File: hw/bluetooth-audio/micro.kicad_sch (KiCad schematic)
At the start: 24 parts, among them J4 Conn_01x02, U1 STM32WB55CGUx, Y1 32MHz, Y2 32.768KHz

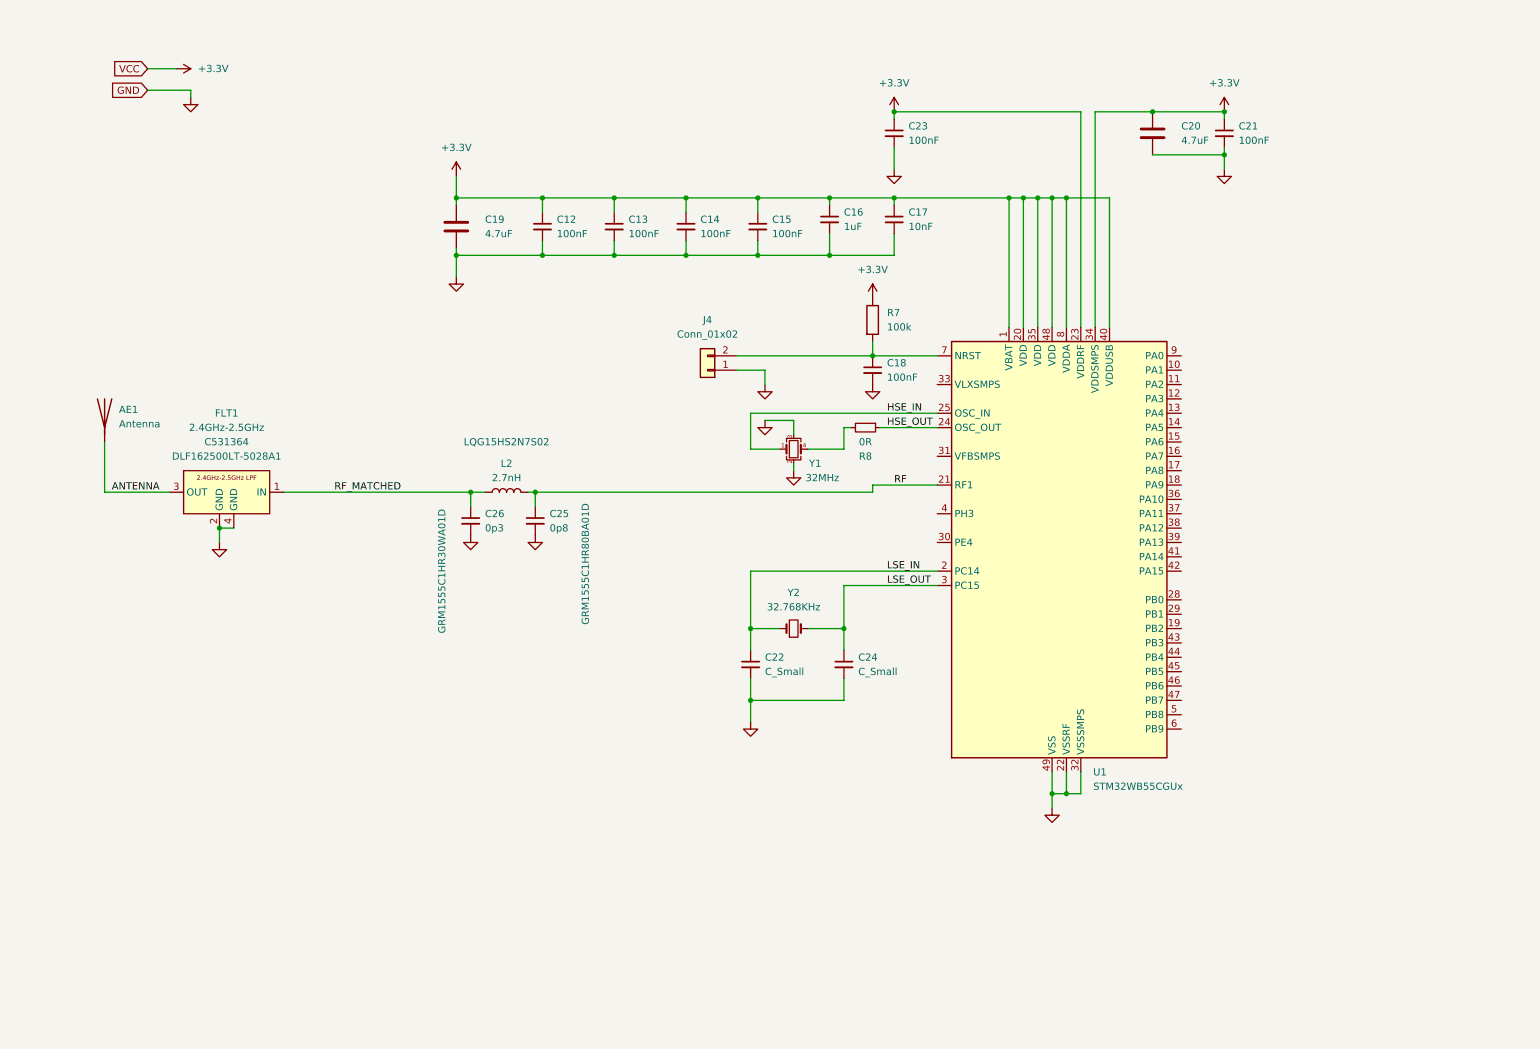
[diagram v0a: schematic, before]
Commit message: Completed design with ESP32D0WD-v3, and JLC production files. High production cost due to req of PCBA standard, due to ESP32 pin pitch.
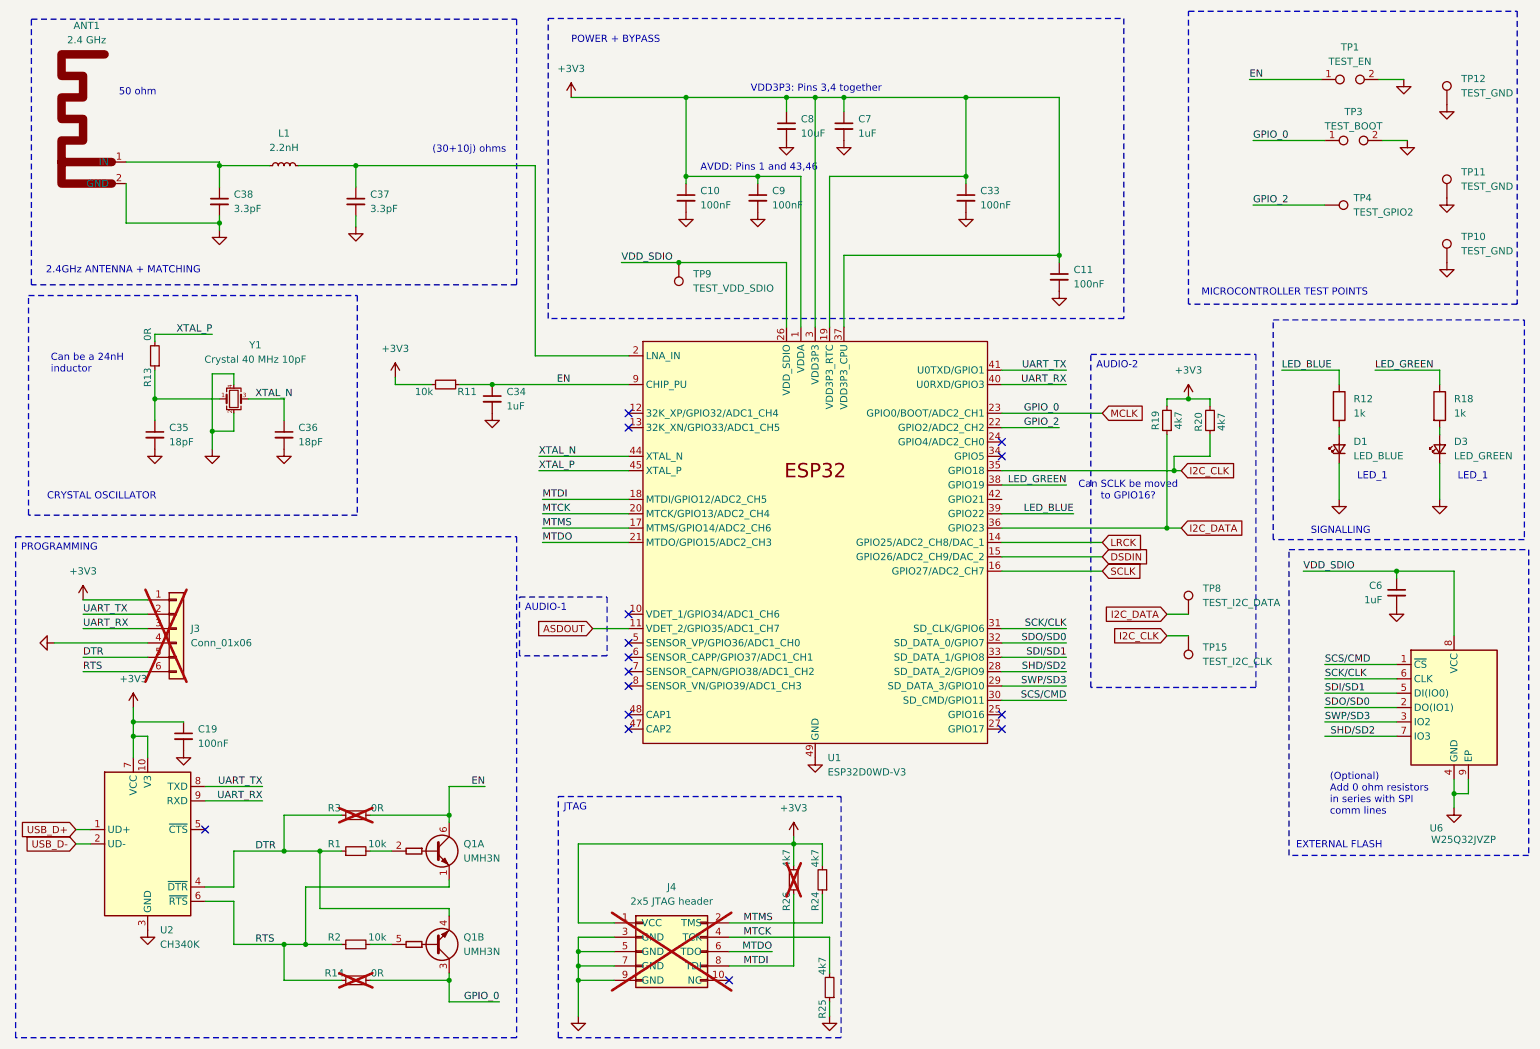
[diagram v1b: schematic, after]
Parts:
- removed AE1: Antenna, symbol Device:Antenna
- removed C12, C13, C14, C15, C18, C21, C23: 100nF, Resistor_SMD:R_0402_1005Metric, symbol Device:C_Small
- removed C16: 1uF, Resistor_SMD:R_0402_1005Metric, symbol Device:C_Small
- removed C17: 10nF, Resistor_SMD:R_0402_1005Metric, symbol Device:C_Small
- removed C19, C20: 4.7uF, Capacitor_SMD:C_0603_1608Metric, symbol Device:C
- removed C22, C24: C_Small, symbol Device:C_Small
- removed C25: 0p8, Inductor_SMD:L_0402_1005Metric, symbol Device:C_Small
- removed C26: 0p3, Inductor_SMD:L_0402_1005Metric, symbol Device:C_Small
- removed FLT1: 2.4GHz-2.5GHz, custom_footprints:DLF162500LT-5028A1, symbol custom_symbols:DLF162500LT-5028A1
- removed J4: Conn_01x02, symbol Connector_Generic:Conn_01x02
- removed L2: 2.7nH, Inductor_SMD:L_0402_1005Metric, symbol Device:L
- removed R7: 100k, symbol Device:R
- removed R8: 0R, symbol Device:R_Small
- removed U1: STM32WB55CGUx, Package_DFN_QFN:QFN-48-1EP_7x7mm_P0.5mm_EP5.6x5.6mm, symbol MCU_ST_STM32WB:STM32WB55CGUx
- removed Y1: 32MHz, symbol Device:Crystal_GND23_Small
- removed Y2: 32.768KHz, symbol Device:Crystal_Small
- added ANT1: 2.4 GHz, custom_footprints:Antenna 2.4GHz Inverted-F Meandered, symbol custom_symbols:Antenna_2.4GHz_Meandered_Inverted-F
- added C10, C11, C19, C33, C9: 100nF, Capacitor_SMD:C_0402_1005Metric, symbol Device:C_Small
- added C34, C6, C7: 1uF, Capacitor_SMD:C_0402_1005Metric, symbol Device:C_Small
- added C35, C36: 18pF, Capacitor_SMD:C_0402_1005Metric, symbol Device:C_Small
- added C37, C38: 3.3pF, Capacitor_SMD:C_0402_1005Metric, symbol Device:C_Small
- added C8: 10uF, Capacitor_SMD:C_0603_1608Metric, symbol Device:C_Small
- added D1: LED_BLUE, LED_SMD:LED_0805_2012Metric, symbol Device:LED_Small
- added D3: LED_GREEN, LED_SMD:LED_0805_2012Metric, symbol Device:LED_Small
- added J3: Conn_01x06, Connector_PinHeader_2.54mm:PinHeader_1x06_P2.54mm_Vertical, symbol Connector_Generic:Conn_01x06
- added J4: 2x5 JTAG header, custom_footprints:2x5 2mm JTAG header pads only, symbol custom_symbols:2x5 JTAG header
- added L1: 2.2nH, Inductor_SMD:L_0402_1005Metric, symbol Device:L_Small
- added Q1: UMH3N, Package_TO_SOT_SMD:SOT-363_SC-70-6, symbol Transistor_BJT:UMH3N
- added R1, R11, R2: 10k, Resistor_SMD:R_0402_1005Metric, symbol Device:R_Small
- added R12, R18: 1k, Resistor_SMD:R_0402_1005Metric, symbol Device:R
- added R13, R14, R3: 0R, Resistor_SMD:R_0402_1005Metric, symbol Device:R_Small
- added R19, R20, R24, R25, R26: 4k7, Resistor_SMD:R_0402_1005Metric, symbol Device:R_Small
- added TP1: TEST_EN, custom_footprints:TestPoint_Pad_2x1_D1.0mm, symbol Connector:TestPoint_2Pole
- added TP10, TP11, TP12: TEST_GND, TestPoint:TestPoint_Pad_D1.0mm, symbol Connector:TestPoint
- added TP15: TEST_I2C_CLK, TestPoint:TestPoint_Pad_D1.0mm, symbol Connector:TestPoint
- added TP3: TEST_BOOT, custom_footprints:TestPoint_Pad_2x1_D1.0mm, symbol Connector:TestPoint_2Pole
- added TP4: TEST_GPIO2, TestPoint:TestPoint_Pad_D1.0mm, symbol Connector:TestPoint
- added TP8: TEST_I2C_DATA, TestPoint:TestPoint_Pad_D1.0mm, symbol Connector:TestPoint
- added TP9: TEST_VDD_SDIO, TestPoint:TestPoint_Pad_D1.0mm, symbol Connector:TestPoint
- added U1: ESP32D0WD-V3, Package_DFN_QFN:QFN-48-1EP_5x5mm_P0.35mm_EP3.7x3.7mm_ThermalVias, symbol PCM_Espressif:ESP32
- added U2: CH340K, Package_SO:SSOP-10-1EP_3.9x4.9mm_P1mm_EP2.1x3.3mm, symbol Interface_USB:CH340K
- added U6: W25Q32JVZP, Package_SON:WSON-8-1EP_6x5mm_P1.27mm_EP3.4x4.3mm, symbol Memory_Flash:W25Q32JVZP
- added Y1: Crystal 40 MHz 10pF, Crystal:Crystal_SMD_SeikoEpson_FA128-4Pin_2.0x1.6mm, symbol Device:Crystal_GND24_Small
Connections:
- net GND: now also ANT1.2 (GND), C10.2, C11.2, C19.2, C33.2, C34.2, C35.2, C36.2, C37.2, C38.2, C6.2, C7.2, C8.2, C9.2, D1.1 (K), D3.1 (K), J3.4 (Pin_4), J4.3 (GND), J4.5 (GND), J4.7 (GND), J4.9 (GND), R25.1, TP1.2, TP10.1, TP11.1, TP12.1, TP3.2, U1.49 (GND), U2.11 (GND), U2.3 (GND), U6.4 (GND), U6.9 (EP), Y1.2, Y1.4
- new net: D3.2 (A), R18.2
- new net: C35.1, R13.1, Y1.1
- new net: Q1.5 (B2), R2.2
- new net: C37.1, L1.2, U1.2 (LNA_IN)
- new net: Q1.2 (B1), R1.2
- new net: D1.2 (A), R12.2
- new net: ANT1.1 (IN), C38.1, L1.1
- new net +3V3: C10.1, C11.1, C19.1, C33.1, C7.1, C8.1, C9.1, J3.1 (Pin_1), J4.1 (VCC), R11.2, R19.2, R20.2, R24.2, R26.2, U1.1 (VDDA), U1.19 (VDD3P3_RTC), U1.3 (VDD3P3), U1.37 (VDD3P3_CPU), U1.4 (VDD3P3), U1.43 (VDDA), U1.46 (VDDA), U2.10 (V3), U2.7 (VCC)
- new net ASDOUT: U1.11 (VDET_2/GPIO35/ADC1_CH7)
- new net DSDIN: U1.15 (GPIO26/ADC2_CH9/DAC_2)
- new net DTR: J3.5 (Pin_5), Q1.4 (E2), R1.1, R3.1, U2.4 (~{DTR})
- new net EN: C34.1, Q1.6 (C1), R11.1, R3.2, TP1.1, U1.9 (CHIP_PU)
- new net GPIO_2: TP4.1, U1.22 (GPIO2/ADC2_CH2)
- new net I2C_CLK: R20.1, TP15.1, U1.35 (GPIO18)
- new net I2C_DATA: R19.1, TP8.1, U1.36 (GPIO23)
- new net LED_BLUE: R12.1, U1.39 (GPIO22)
- new net LED_GREEN: R18.1, U1.38 (GPIO19)
- new net LRCK: U1.14 (GPIO25/ADC2_CH8/DAC_1)
- new net MCLK: Q1.3 (C2), R14.2, TP3.1, U1.23 (GPIO0/BOOT/ADC2_CH1)
- new net MTCK: J4.4 (TCK), R25.2, U1.20 (MTCK/GPIO13/ADC2_CH4)
- new net MTDI: J4.8 (TDI), R26.1, U1.18 (MTDI/GPIO12/ADC2_CH5)
- new net MTDO: J4.6 (TDO), U1.21 (MTDO/GPIO15/ADC2_CH3)
- new net MTMS: J4.2 (TMS), R24.1, U1.17 (MTMS/GPIO14/ADC2_CH6)
- new net RTS: J3.6 (Pin_6), Q1.1 (E1), R14.1, R2.1, U2.6 (~{RTS})
- new net SCK/CLK: U1.31 (SD_CLK/GPIO6), U6.6 (CLK)
- new net SCLK: U1.16 (GPIO27/ADC2_CH7)
- new net SCS/CMD: U1.30 (SD_CMD/GPIO11), U6.1 (~{CS})
- new net SDI/SD1: U1.33 (SD_DATA_1/GPIO8), U6.5 (DI(IO0))
- new net SDO/SD0: U1.32 (SD_DATA_0/GPIO7), U6.2 (DO(IO1))
- new net SHD/SD2: U1.28 (SD_DATA_2/GPIO9), U6.7 (IO3)
- new net SWP/SD3: U1.29 (SD_DATA_3/GPIO10), U6.3 (IO2)
- new net UART_RX: J3.3 (Pin_3), U1.40 (U0RXD/GPIO3), U2.9 (RXD)
- new net UART_TX: J3.2 (Pin_2), U1.41 (U0TXD/GPIO1), U2.8 (TXD)
- new net USB_D+: U2.1 (UD+)
- new net USB_D-: U2.2 (UD-)
- new net VDD_SDIO: C6.1, TP9.1, U1.26 (VDD_SDIO), U6.8 (VCC)
- new net XTAL_N: C36.1, U1.44 (XTAL_N), Y1.3
- new net XTAL_P: R13.2, U1.45 (XTAL_P)
- no-connect marks 0 -> 15
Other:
- note added: "(30+10j) ohms"
- note added: "(Optional) Add 0 ohm resistors in series with SPI comm lines"
- note added: "2.4GHz ANTENNA + MATCHING"
- note added: "50 ohm"
- note added: "AVDD: Pins 1 and 43,46"
- note added: "CRYSTAL OSCILLATOR"
- note added: "Can SCLK be moved to GPIO16?"
- note added: "Can be a 24nH inductor"
- note added: "EXTERNAL FLASH"
- note added: "LED_1"
- note added: "MICROCONTROLLER TEST POINTS"
- note added: "POWER + BYPASS"
- note added: "SIGNALLING"
- note added: "VDD3P3: Pins 3,4 together"

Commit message: Custom symbol and footprints for IS2083. Updated design document. Initial dump of components onto cleared PCB.
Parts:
- removed C10, C11, C19, C33, C9: 100nF, Capacitor_SMD:C_0402_1005Metric, symbol Device:C_Small
- removed C34, C6, C7: 1uF, Capacitor_SMD:C_0402_1005Metric, symbol Device:C_Small
- removed C35, C36: 18pF, Capacitor_SMD:C_0402_1005Metric, symbol Device:C_Small
- removed C8: 10uF, Capacitor_SMD:C_0603_1608Metric, symbol Device:C_Small
- removed J3: Conn_01x06, Connector_PinHeader_2.54mm:PinHeader_1x06_P2.54mm_Vertical, symbol Connector_Generic:Conn_01x06
- removed Q1: UMH3N, Package_TO_SOT_SMD:SOT-363_SC-70-6, symbol Transistor_BJT:UMH3N
- removed R1, R11, R2: 10k, Resistor_SMD:R_0402_1005Metric, symbol Device:R_Small
- removed R13, R14, R3: 0R, Resistor_SMD:R_0402_1005Metric, symbol Device:R_Small
- removed R19, R20: 4k7, Resistor_SMD:R_0402_1005Metric, symbol Device:R_Small
- removed TP15: TEST_I2C_CLK, TestPoint:TestPoint_Pad_D1.0mm, symbol Connector:TestPoint
- removed TP8: TEST_I2C_DATA, TestPoint:TestPoint_Pad_D1.0mm, symbol Connector:TestPoint
- removed TP9: TEST_VDD_SDIO, TestPoint:TestPoint_Pad_D1.0mm, symbol Connector:TestPoint
- removed U1: ESP32D0WD-V3, Package_DFN_QFN:QFN-48-1EP_5x5mm_P0.35mm_EP3.7x3.7mm_ThermalVias, symbol PCM_Espressif:ESP32
- removed U2: CH340K, Package_SO:SSOP-10-1EP_3.9x4.9mm_P1mm_EP2.1x3.3mm, symbol Interface_USB:CH340K
- removed U6: W25Q32JVZP, Package_SON:WSON-8-1EP_6x5mm_P1.27mm_EP3.4x4.3mm, symbol Memory_Flash:W25Q32JVZP
- removed Y1: Crystal 40 MHz 10pF, Crystal:Crystal_SMD_SeikoEpson_FA128-4Pin_2.0x1.6mm, symbol Device:Crystal_GND24_Small
- added U2: IS2083BM-232, custom_footprints:VFBGA82_3MX_MCH, symbol IS2083 Bluetooth Audio SoC:IS2083BM-232
- renumbered ANT1 to ANT2, C38 to C46, C37 to C48, D1 to D4, D3 to D5, J4 to J6, L1 to L2, R26 to R30, R24 to R31, R25 to R32, R12 to R35, R18 to R36, TP4 to TP19, TP1 to TP20, TP3 to TP21, TP12 to TP22, TP11 to TP23, TP10 to TP24
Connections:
- net GPIO_2: no longer names the net of TP19.1
- net MCLK: no longer names the net of TP21.1
- no-connect marks 15 -> 1
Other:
- note removed: "(Optional) Add 0 ohm resistors in series with SPI comm lines"
- note removed: "AVDD: Pins 1 and 43,46"
- note removed: "Can SCLK be moved to GPIO16?"
- note removed: "Can be a 24nH inductor"
- note removed: "EXTERNAL FLASH"
- note removed: "VDD3P3: Pins 3,4 together"
- moved on the sheet: ANT2, C46, C48, D4, D5, J6, L2, R30, R31, R32, R35, R36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
